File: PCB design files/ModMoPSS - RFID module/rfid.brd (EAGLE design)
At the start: 100 x 55 mm, 76 parts, among them IC1 LT1761, IC2 7805_TO252, IC3 EM4095, IC4 EM4095, IC5 LT1761

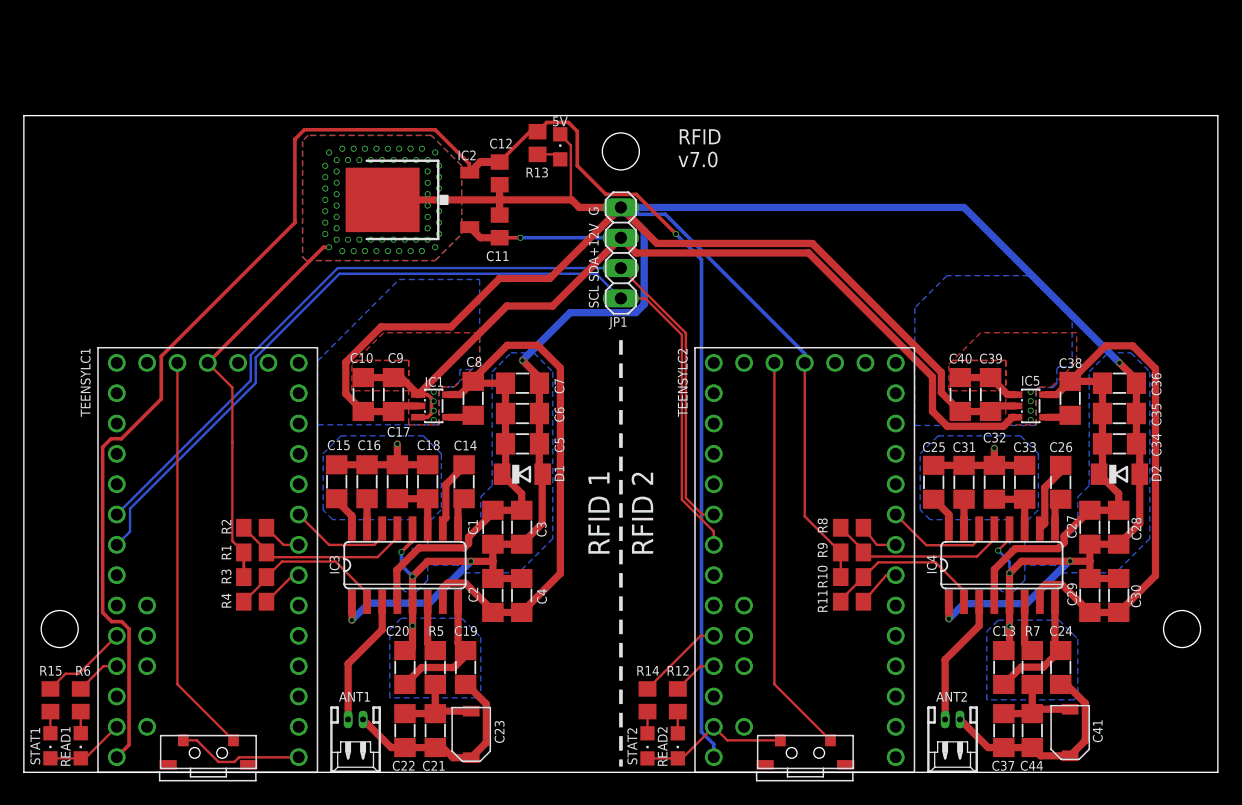
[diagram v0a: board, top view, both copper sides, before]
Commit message: Fix for non functional level shifting
Update to fix non functional level shifting on DMOD and CLK pins
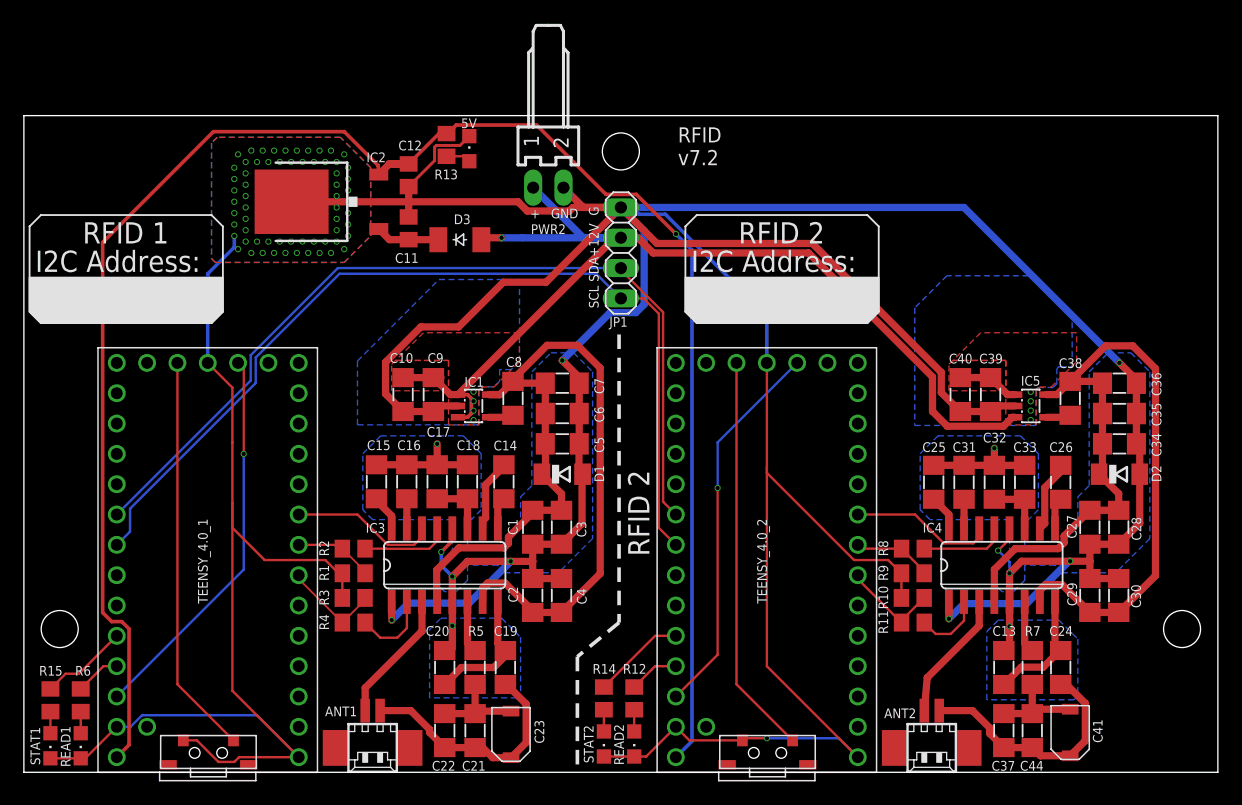
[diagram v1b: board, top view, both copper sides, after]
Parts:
- removed TEENSYLC1, TEENSYLC2: TEENSYLC, 000-my_library:TEENSYLC
- added D3: SM4007PL, diode:SOD-123_MINI-SMA
- added PWR2: 22-05-7028-02, con-molex:7395-02
- added TEENSY_4.0_1, TEENSY_4.0_2: TEENSY40, 000-my_library:TEENSY40
- ANT1, ANT2: value 53048-02 -> 53261-02; device con-molex:53048-02 -> con-molex:53261-02
- moved R1 8.44 mm to (27.6, 16.7)
- moved R2 8.44 mm to (27.6, 18.7), turned to 0 degrees
- moved R3 8.44 mm to (27.6, 14.6)
- moved R4 8.44 mm to (27.6, 12.5), turned to 0 degrees
- moved 5V 7.62 mm to (37.3, 52.2)
- moved IC2 7.62 mm to (24.9, 47.8)
- moved R13 7.62 mm to (35.4, 52.5)
- moved C11 7.62 mm to (32.2, 45.6)
- moved C12 7.62 mm to (32.2, 50.0)
- moved R11 5.38 mm to (74.5, 12.5), turned to 0 degrees
- moved R8 5.38 mm to (74.5, 18.7), turned to 0 degrees
- moved R10 5.37 mm to (74.4, 14.6)
- moved R9 5.37 mm to (74.4, 16.7)
- moved R12 3.65 mm to (51.1, 6.19)
- moved R14 3.65 mm to (48.6, 6.19)
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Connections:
- net ANT1 renamed N$20
- removed net DMOD: IC3.13, R1.1, R2.2
- removed net DMOD1: IC4.13, R8.2, R9.1
- removed net RDY/CLK: IC3.2, R3.1, R4.2
- removed net RDY/CLK1: IC4.2, R10.1, R11.2
- new net N$21: C11.1, D3.C, IC2.1
- new net N$22: IC4.13, R8.2
- new net N$23: IC3.2, R4.2
- new net N$24: IC3.13, R2.2
- new net N$26: IC4.2, R11.2
- net +12V: now also D3.A, PWR2.1; no longer C11.1, IC2.1
- net +5V: now also TEENSY_4.0_1.VIN, TEENSY_4.0_2.VIN; no longer TEENSYLC1.VIN, TEENSYLC2.VIN
- net GND: now also PWR2.2, TEENSY_4.0_1.GND, TEENSY_4.0_1.GND@1, TEENSY_4.0_1.GND@2, TEENSY_4.0_2.GND, TEENSY_4.0_2.GND@1, TEENSY_4.0_2.GND@2; no longer TEENSYLC1.GND, TEENSYLC1.GND@1, TEENSYLC1.GND@2, TEENSYLC2.GND, TEENSYLC2.GND@1, TEENSYLC2.GND@2
- net LED1: now also TEENSY_4.0_1.23; no longer TEENSYLC1.23
- net LED2: now also TEENSY_4.0_2.23; no longer TEENSYLC2.23
- net N$10: now also TEENSY_4.0_1.3V3, TEENSY_4.0_1.3V3@2; no longer TEENSYLC1.3V3, TEENSYLC1.3V3@2
- net N$11: now also R9.1, TEENSY_4.0_2.6; no longer TEENSYLC2.6
- net N$12: now also R10.1, TEENSY_4.0_2.5; no longer TEENSYLC2.5
- net N$15: now also TEENSY_4.0_1.7; no longer TEENSYLC1.7
- net N$16: now also TEENSY_4.0_2.PROG; no longer TEENSYLC2.PROG
- net N$17: now also TEENSY_4.0_2.3V3, TEENSY_4.0_2.3V3@2; no longer TEENSYLC2.3V3, TEENSYLC2.3V3@2
- net N$2: now also R3.1, TEENSY_4.0_1.5; no longer TEENSYLC1.5
- net N$6: now also R1.1, TEENSY_4.0_1.6; no longer TEENSYLC1.6
- net N$8: now also TEENSY_4.0_1.PROG; no longer TEENSYLC1.PROG
- net SCL: now also TEENSY_4.0_1.19, TEENSY_4.0_2.19; no longer TEENSYLC1.19, TEENSYLC2.19
- net SDA: now also TEENSY_4.0_1.18, TEENSY_4.0_2.18; no longer TEENSYLC1.18, TEENSYLC2.18
- net SHD1: now also TEENSY_4.0_2.7; no longer TEENSYLC2.7
- net STAT1: now also TEENSY_4.0_1.22; no longer TEENSYLC1.22
- net STAT2: now also TEENSY_4.0_2.22; no longer TEENSYLC2.22
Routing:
- net GND: track 412.6 -> 512.6 mm, vias 78 -> 79
- net N$10: track 0.00 -> 32.5 mm, vias 0 -> 1
- net N$17: track 0.00 -> 32.1 mm, vias 0 -> 1
- net DMOD: track 15.5 -> 0.00 mm
- net DMOD1: track 15.5 -> 0.00 mm
- net RDY/CLK: track 13.7 -> 0.00 mm
- net RDY/CLK1: track 13.7 -> 0.00 mm
- net N$24: track 0.00 -> 7.37 mm
- net N$22: track 0.00 -> 7.19 mm
- net N$23: track 0.00 -> 6.56 mm
- net N$26: track 0.00 -> 5.76 mm
- net N$21: track 0.00 -> 5.36 mm
- net +12V: track 91.1 -> 96.3 mm
- net N$2: track 3.62 -> 8.33 mm
- net N$12: track 3.72 -> 8.33 mm
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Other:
- board text added: "+"
- board text added: "GND"
- board text added: "I2C Address:"
- board text added: "RFID v7.2"
- board text removed: "RFID v7.0"
